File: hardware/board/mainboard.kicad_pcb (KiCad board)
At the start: 4 copper layers, 60 x 110 mm, 266 parts, among them J201 Power, Q601 BCM847, Q701 BCM847, Q801 BCM847, U1 TL074, U2 TL074, U201 TL431A, U3 TL074, U4 TL074, U5 TL074, U6 TL074

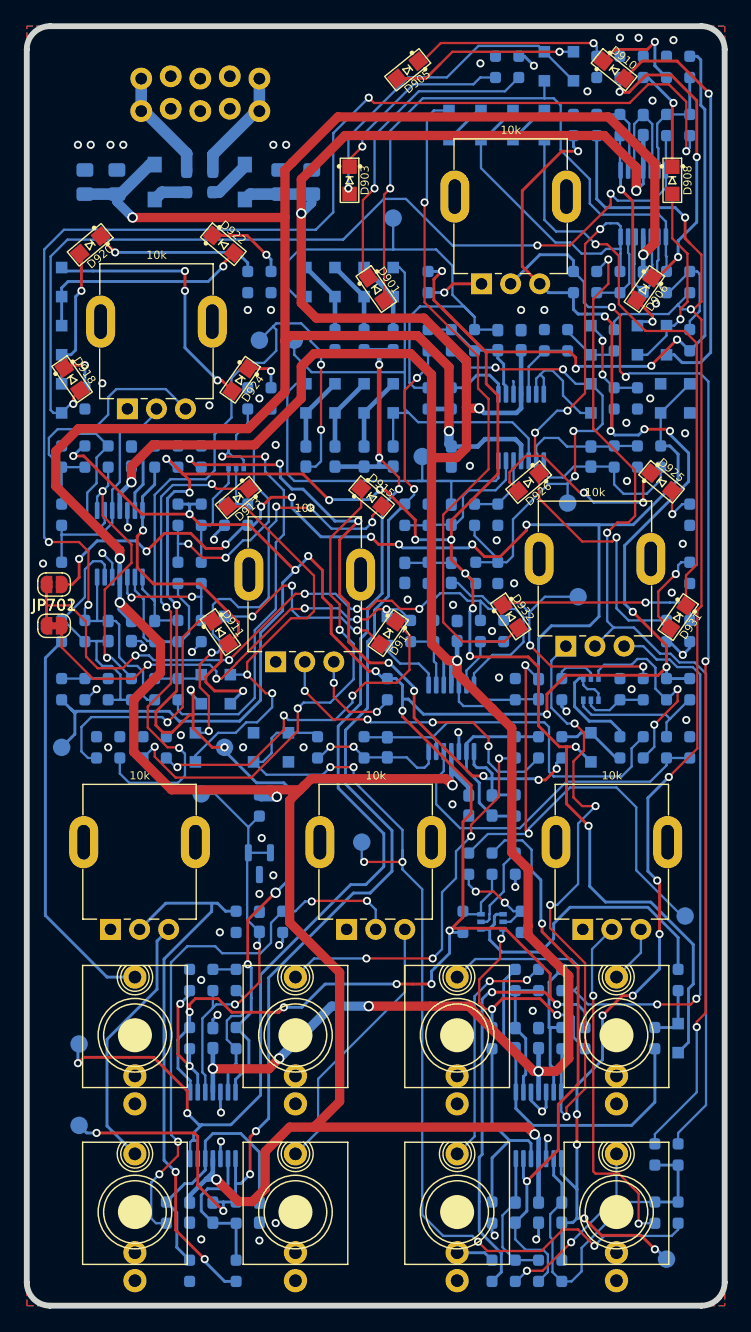
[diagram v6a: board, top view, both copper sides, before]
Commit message: hardware: minor routing changes: pull some vias back from the board edge, move test points, move vias back from pot mounting pads
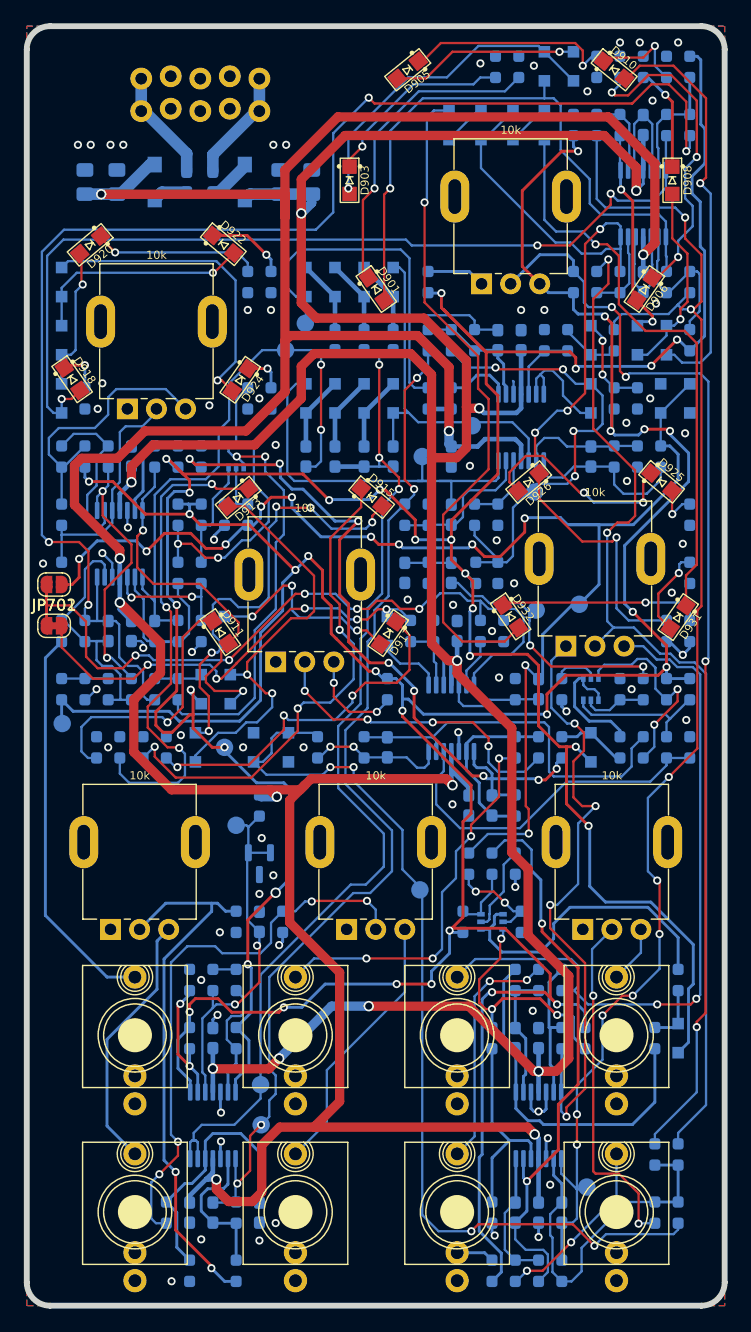
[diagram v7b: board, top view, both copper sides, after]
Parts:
- moved TP508 28.3 mm to (98.2, 100.0)
- moved TP507 17.0 mm to (89.0, 84.6)
- moved TP504 16.0 mm to (70.8, 141.2)
- moved TP502 15.7 mm to (70.8, 144.7)
- moved TP505 11.8 mm to (74.7, 75.8)
- moved TP401 9.24 mm to (98.8, 150.1)
- moved TP702 6.47 mm to (84.5, 124.5)
- moved TP201 4.04 mm to (68.7, 119.0)
- moved TP701 3.78 mm to (94.5, 100.5)
- moved TP501 3.00 mm to (94.3, 90.3)
- moved TP503 2.41 mm to (73.0, 78.1)
- moved TP202 2.05 mm to (53.8, 110.2)
- turned R401 to -90 degrees
- turned R602 to -90 degrees
- turned R616 to 90 degrees
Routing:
- net /Filter Core/OUT: track 141.0 -> 116.4 mm
- net /Filter Core/LOW_PASS_IN: track 108.0 -> 89.4 mm, vias 6 -> 4
- net /Filter Core/HIGH_PASS_IN: track 109.4 -> 93.5 mm, vias 5 -> 3
- net Net-(D506-K): track 42.1 -> 30.7 mm
- net /Cutoff CV Driver/CUTOFF_OUT: track 133.5 -> 125.0 mm, vias 11 -> 9
- net /Cutoff CV Driver/INSTABILITY_IN: track 89.5 -> 81.9 mm, vias 6 -> 4
- net /Filter Core/RESONANCE_IN: track 56.5 -> 50.7 mm
- net Net-(D503-A): track 44.0 -> 38.7 mm
- net +8VREF: track 286.5 -> 281.8 mm
- net /Power/2.5v unbuffered: track 36.6 -> 32.3 mm
- net Net-(C703-Pad1): track 26.9 -> 23.3 mm
- net Net-(D923-K): track 22.9 -> 26.3 mm, vias 3 -> 1
- net Net-(D918-A): track 81.9 -> 79.0 mm
- net Net-(Q601-E-Pad1): track 38.4 -> 35.7 mm
- net Net-(D502-K): track 43.8 -> 41.6 mm
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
